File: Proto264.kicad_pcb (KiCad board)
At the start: 2 copper layers, 99.8 x 99.9 mm, 5 parts, among them CN1 C16-Exp-Port, J1 PIN_HEADER, J2 PIN_HEADER_GND, J3 PIN_HEADER_VCC, J4 PROTO_AREA

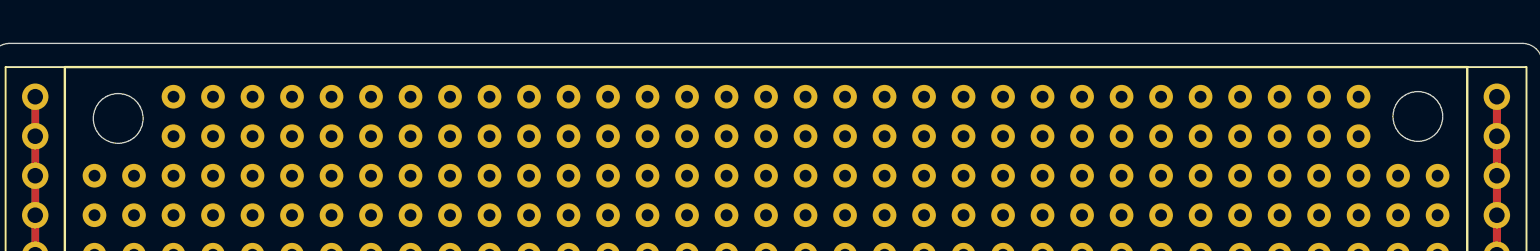
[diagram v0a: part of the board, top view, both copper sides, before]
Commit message: Added mounting points without copper
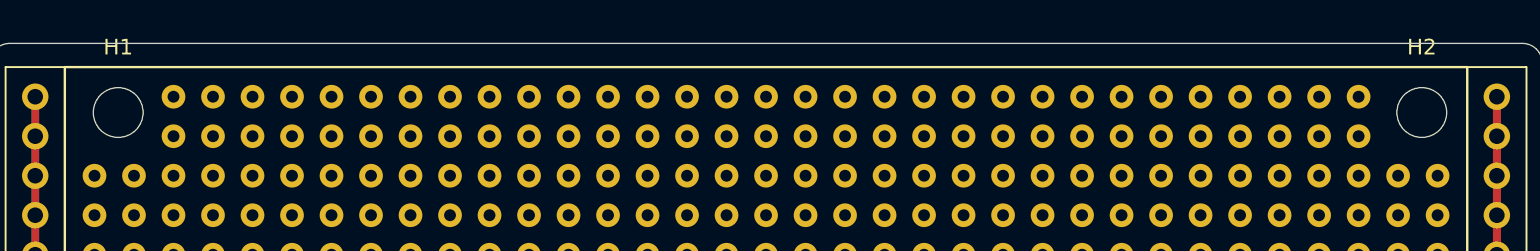
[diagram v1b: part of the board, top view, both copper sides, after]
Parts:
- added H1: MountingHole, MountingHole:MountingHole_3.2mm_M3, F.Cu at (110.5, 52.6)
- added H2: MountingHole, MountingHole:MountingHole_3.2mm_M3, F.Cu at (194.3, 52.6)
